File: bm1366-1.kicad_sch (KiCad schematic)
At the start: 64 parts, among them U1 25MHz, U13 ADP171AUJ-R7, U14 BM1366_mode1, U23 ADP171AUJ-R7

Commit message: added some DK part numbers
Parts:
- R6: DK (none) -> 311-10KJRCT-ND; PARTNO (none) -> RC0402JR-0710KL
- U13, U23: DK (none) -> 505-ADP171AUJZ-R7CT-ND; PARTNO (none) -> ADP171AUJZ-R7
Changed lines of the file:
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@@
+      (effects (font (size 1.27 1.27)) hide)
+    )
+    (property "DK" "505-ADP171AUJZ-R7CT-ND" (at 62.865 177.165 0)
+      (effects (font (size 1.27 1.27)) hide)
+    )
+    (property "PARTNO" "ADP171AUJZ-R7" (at 62.865 177.165 0)
       (effects (font (size 1.27 1.27)) hide)
     )
@@
       (effects (font (size 1.27 1.27)) hide)
     )
+    (property "DK" "505-ADP171AUJZ-R7CT-ND" (at 62.865 144.145 0)
+      (effects (font (size 1.27 1.27)) hide)
+    )
+    (property "PARTNO" "ADP171AUJZ-R7" (at 62.865 144.145 0)
+      (effects (font (size 1.27 1.27)) hide)
+    )
     (pin "1")
     (pin "2")
@@
       (effects (font (size 1.27 1.27)) hide)
     )
-    (property "DK" "" (at 18.415 92.71 0)
-      (effects (font (size 1.27 1.27)) hide)
-    )
-    (property "PARTNO" "" (at 18.415 92.71 0)
-      (effects (font (size 1.27 1.27)) hide)
-    )
+    (property "DK" "311-10KJRCT-ND" (at 18.415 92.71 0)
+      (effects (font (size 1.27 1.27)) hide)
+    )
+    (property "PARTNO" "RC0402JR-0710KL" (at 18.415 92.71 0)
+      (effects (font (size 1.27 1.27)) hide)
+    )

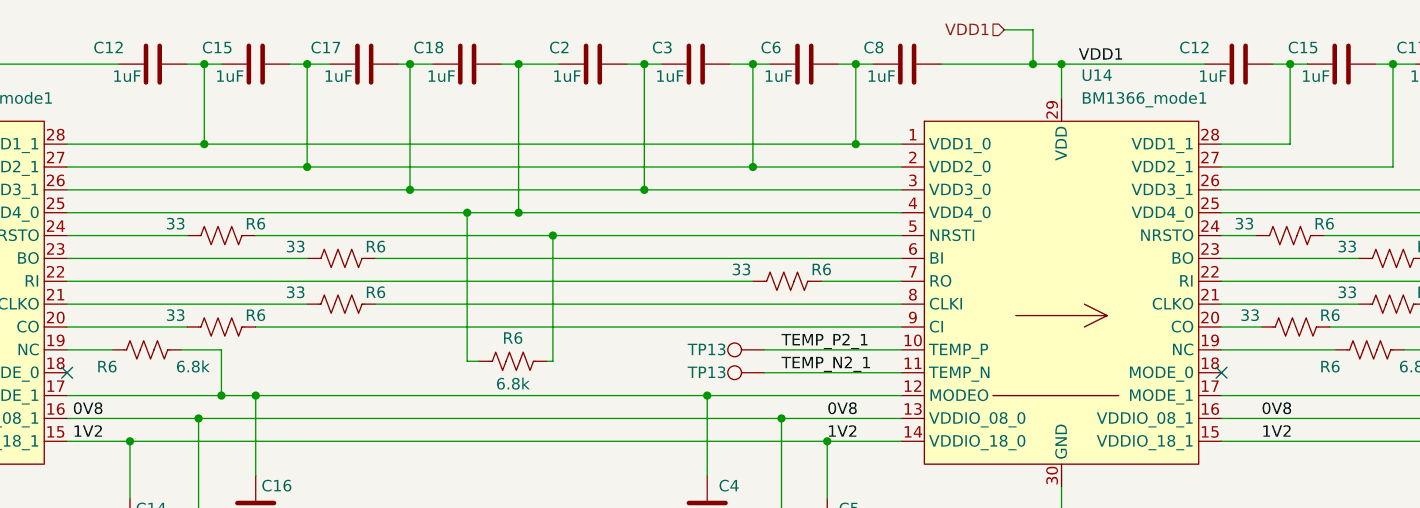
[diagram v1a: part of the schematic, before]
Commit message: Add ESP32 testpoints, fix all DRC errors
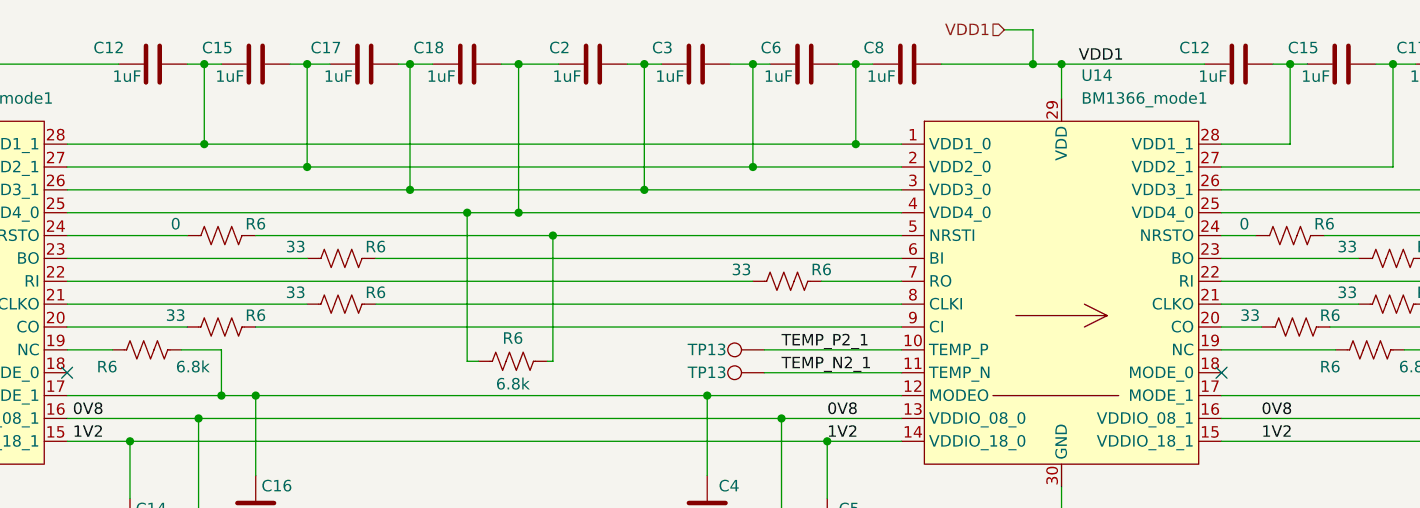
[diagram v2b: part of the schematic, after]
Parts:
- R6: value 33 -> 0
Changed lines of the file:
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@@
       (effects (font (size 1.27 1.27)))
     )
-    (property "Value" "33" (at 102.235 83.82 90)
+    (property "Value" "0" (at 102.235 83.82 90)
       (effects (font (size 1.27 1.27)))
     )
@@
       (effects (font (size 1.27 1.27)))
     )
-    (property "Value" "33" (at 220.98 83.82 90)
-      (effects (font (size 1.27 1.27)))
-    )
+    (property "Value" "0" (at 220.98 83.82 90)
+      (effects (font (size 1.27 1.27)))
+    )

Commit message: BOM mostly completed
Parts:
- R35, R36: DK (none) -> 311-1.00LRCT-ND; PARTNO (none) -> RC0402FR-071RL
- R6: value 130K -> 130k 1%; DK (none) -> YAG2969CT-ND; PARTNO (none) -> RC0402FR-07130KL; Tolerance 1% -> (none)
- R6: DK (none) -> 311-33.0LRCT-ND; PARTNO (none) -> RC0402FR-0733RL
- R6: DK (none) -> 13-RC0402FR-136K8LCT-ND; PARTNO (none) -> RC0402FR-136K8L
- R6: value 182K -> 182k 1%; DK (none) -> YAG3015CT-ND; PARTNO (none) -> RC0402FR-07182KL; Tolerance 1% -> (none)
- R6: DK (none) -> 311-0.0JRCT-ND; PARTNO (none) -> RC0402JR-070RL
- R6: value 309K -> 309k 1%; DK (none) -> YAG3108CT-ND; PARTNO (none) -> RC0402FR-07309KL; Tolerance 1% -> (none)
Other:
- title: bitaxeUltraHex -> bitaxeHex
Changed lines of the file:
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@@
   (paper "A")
   (title_block
-    (title "bitaxeUltraHex")
+    (title "bitaxeHex")
     (date "2023-06-11")
-    (rev "1")
+    (rev "300")
   )
   (junction (at 50.165 194.31) (diameter 0) (color 0 0 0 0)
@@
       (effects (font (size 1.27 1.27)))
     )
-    (property "Value" "130K" (at 71.12 189.865 0)
+    (property "Value" "130k 1%" (at 71.12 189.865 0)
       (effects (font (size 1.27 1.27)))
     )
@@
       (effects (font (size 1.27 1.27)) hide)
     )
-    (property "DK" "" (at 74.93 187.96 0)
+    (property "DK" "YAG2969CT-ND" (at 74.93 187.96 0)
       (effects (font (size 1.27 1.27)) hide)
     )
-    (property "PARTNO" "" (at 74.93 187.96 0)
+    (property "PARTNO" "RC0402FR-07130KL" (at 74.93 187.96 0)
       (effects (font (size 1.27 1.27)) hide)
     )
-    (property "Tolerance" "1%" (at 71.755 191.77 0)
-      (effects (font (size 1.27 1.27)))
-    )
     (pin "1")
     (pin "2")
@@
       (effects (font (size 1.27 1.27)) hide)
     )
-    (property "DK" "" (at 120.65 87.63 0)
+    (property "DK" "311-33.0LRCT-ND" (at 120.65 87.63 0)
       (effects (font (size 1.27 1.27)) hide)
     )
-    (property "PARTNO" "" (at 120.65 87.63 0)
+    (property "PARTNO" "RC0402FR-0733RL" (at 120.65 87.63 0)
       (effects (font (size 1.27 1.27)) hide)
     )
@@
       (effects (font (size 1.27 1.27)) hide)
     )
-    (property "DK" "" (at 139.7 99.06 0)
+    (property "DK" "13-RC0402FR-136K8LCT-ND" (at 139.7 99.06 0)
       (effects (font (size 1.27 1.27)) hide)
     )
-    (property "PARTNO" "" (at 139.7 99.06 0)
+    (property "PARTNO" "RC0402FR-136K8L" (at 139.7 99.06 0)
       (effects (font (size 1.27 1.27)) hide)
     )
@@
       (effects (font (size 1.27 1.27)) hide)
     )
-    (property "DK" "" (at 234.95 97.79 0)
+    (property "DK" "13-RC0402FR-136K8LCT-ND" (at 234.95 97.79 0)
       (effects (font (size 1.27 1.27)) hide)
     )
-    (property "PARTNO" "" (at 234.95 97.79 0)
+    (property "PARTNO" "RC0402FR-136K8L" (at 234.95 97.79 0)
       (effects (font (size 1.27 1.27)) hide)
     )
@@
       (effects (font (size 1.27 1.27)) hide)
     )
-    (property "DK" "" (at 99.06 97.79 0)
+    (property "DK" "13-RC0402FR-136K8LCT-ND" (at 99.06 97.79 0)
       (effects (font (size 1.27 1.27)) hide)
     )
-    (property "PARTNO" "" (at 99.06 97.79 0)
+    (property "PARTNO" "RC0402FR-136K8L" (at 99.06 97.79 0)
       (effects (font (size 1.27 1.27)) hide)
     )
@@
       (effects (font (size 1.27 1.27)))
     )
-    (property "Value" "182K" (at 81.28 183.515 90)
+    (property "Value" "182k 1%" (at 81.28 183.515 90)
       (effects (font (size 1.27 1.27)))
     )
@@
       (effects (font (size 1.27 1.27)) hide)
     )
-    (property "DK" "" (at 81.28 180.975 0)
+    (property "DK" "YAG3015CT-ND" (at 81.28 180.975 0)
       (effects (font (size 1.27 1.27)) hide)
     )
-    (property "PARTNO" "" (at 81.28 180.975 0)
+    (property "PARTNO" "RC0402FR-07182KL" (at 81.28 180.975 0)
       (effects (font (size 1.27 1.27)) hide)
     )
-    (property "Tolerance" "1%" (at 81.28 185.42 90)
-      (effects (font (size 1.27 1.27)))
-    )
     (pin "1")
     (pin "2")
@@
       (effects (font (size 1.27 1.27)) hide)
     )
-    (property "DK" "" (at 107.315 85.09 0)
+    (property "DK" "311-0.0JRCT-ND" (at 107.315 85.09 0)
       (effects (font (size 1.27 1.27)) hide)
     )
-    (property "PARTNO" "" (at 107.315 85.09 0)
+    (property "PARTNO" "RC0402JR-070RL" (at 107.315 85.09 0)
       (effects (font (size 1.27 1.27)) hide)
     )
@@
       (effects (font (size 1.27 1.27)) hide)
     )
+    (property "DK" "311-1.00LRCT-ND" (at 131.445 180.34 0)
+      (effects (font (size 1.27 1.27)) hide)
+    )
+    (property "PARTNO" "RC0402FR-071RL" (at 131.445 180.34 0)
+      (effects (font (size 1.27 1.27)) hide)
+    )
     (pin "1")
     (pin "2")
@@
       (effects (font (size 1.27 1.27)) hide)
     )
-    (property "DK" "" (at 237.49 87.63 0)
+    (property "DK" "311-33.0LRCT-ND" (at 237.49 87.63 0)
       (effects (font (size 1.27 1.27)) hide)
     )
-    (property "PARTNO" "" (at 237.49 87.63 0)
+    (property "PARTNO" "RC0402FR-0733RL" (at 237.49 87.63 0)
       (effects (font (size 1.27 1.27)) hide)
     )
@@
       (effects (font (size 1.27 1.27)) hide)
     )
-    (property "DK" "" (at 107.315 95.25 0)
+    (property "DK" "311-33.0LRCT-ND" (at 107.315 95.25 0)
       (effects (font (size 1.27 1.27)) hide)
     )
-    (property "PARTNO" "" (at 107.315 95.25 0)
+    (property "PARTNO" "RC0402FR-0733RL" (at 107.315 95.25 0)
       (effects (font (size 1.27 1.27)) hide)
     )
@@
       (effects (font (size 1.27 1.27)) hide)
     )
-    (property "DK" "" (at 120.65 92.71 0)
+    (property "DK" "311-33.0LRCT-ND" (at 120.65 92.71 0)
       (effects (font (size 1.27 1.27)) hide)
     )
-    (property "PARTNO" "" (at 120.65 92.71 0)
+    (property "PARTNO" "RC0402FR-0733RL" (at 120.65 92.71 0)
       (effects (font (size 1.27 1.27)) hide)
     )
@@
       (effects (font (size 1.27 1.27)) hide)
     )
-    (property "DK" "" (at 226.695 95.25 0)
+    (property "DK" "311-33.0LRCT-ND" (at 226.695 95.25 0)
       (effects (font (size 1.27 1.27)) hide)
     )
-    (property "PARTNO" "" (at 226.695 95.25 0)
+    (property "PARTNO" "RC0402FR-0733RL" (at 226.695 95.25 0)
       (effects (font (size 1.27 1.27)) hide)
     )
@@
       (effects (font (size 1.27 1.27)) hide)
     )
-    (property "DK" "" (at 226.06 85.09 0)
+    (property "DK" "311-0.0JRCT-ND" (at 226.06 85.09 0)
       (effects (font (size 1.27 1.27)) hide)
     )
-    (property "PARTNO" "" (at 226.06 85.09 0)
+    (property "PARTNO" "RC0402JR-070RL" (at 226.06 85.09 0)
       (effects (font (size 1.27 1.27)) hide)
     )
@@
       (effects (font (size 1.27 1.27)) hide)
     )
+    (property "DK" "311-1.00LRCT-ND" (at 122.555 180.34 0)
+      (effects (font (size 1.27 1.27)) hide)
+    )
+    (property "PARTNO" "RC0402FR-071RL" (at 122.555 180.34 0)
+      (effects (font (size 1.27 1.27)) hide)
+    )
     (pin "1")
     (pin "2")
@@
       (effects (font (size 1.27 1.27)) hide)
     )
-    (property "DK" "" (at 237.49 92.71 0)
+    (property "DK" "311-33.0LRCT-ND" (at 237.49 92.71 0)
       (effects (font (size 1.27 1.27)) hide)
     )
-    (property "PARTNO" "" (at 237.49 92.71 0)
+    (property "PARTNO" "RC0402FR-0733RL" (at 237.49 92.71 0)
       (effects (font (size 1.27 1.27)) hide)
     )
@@
       (effects (font (size 1.27 1.27)))
     )
-    (property "Value" "182K" (at 81.28 150.495 90)
+    (property "Value" "182k 1%" (at 81.28 150.495 90)
       (effects (font (size 1.27 1.27)))
     )
@@
       (effects (font (size 1.27 1.27)) hide)
     )
-    (property "DK" "" (at 81.28 147.955 0)
+    (property "DK" "YAG3015CT-ND" (at 81.28 147.955 0)
       (effects (font (size 1.27 1.27)) hide)
     )
-    (property "PARTNO" "" (at 81.28 147.955 0)
+    (property "PARTNO" "RC0402FR-07182KL" (at 81.28 147.955 0)
       (effects (font (size 1.27 1.27)) hide)
     )
-    (property "Tolerance" "1%" (at 81.28 152.4 90)
-      (effects (font (size 1.27 1.27)))
-    )
     (pin "1")
     (pin "2")
@@
       (effects (font (size 1.27 1.27)) hide)
     )
-    (property "DK" "" (at 170.18 90.17 0)
+    (property "DK" "311-33.0LRCT-ND" (at 170.18 90.17 0)
       (effects (font (size 1.27 1.27)) hide)
     )
-    (property "PARTNO" "" (at 170.18 90.17 0)
+    (property "PARTNO" "RC0402FR-0733RL" (at 170.18 90.17 0)
       (effects (font (size 1.27 1.27)) hide)
     )
@@
       (effects (font (size 1.27 1.27)))
     )
-    (property "Value" "309K" (at 71.12 156.845 0)
+    (property "Value" "309k 1%" (at 71.12 156.845 0)
       (effects (font (size 1.27 1.27)))
     )
@@
       (effects (font (size 1.27 1.27)) hide)
     )
-    (property "DK" "" (at 74.93 154.94 0)
+    (property "DK" "YAG3108CT-ND" (at 74.93 154.94 0)
       (effects (font (size 1.27 1.27)) hide)
     )
-    (property "PARTNO" "" (at 74.93 154.94 0)
+    (property "PARTNO" "RC0402FR-07309KL" (at 74.93 154.94 0)
       (effects (font (size 1.27 1.27)) hide)
     )
-    (property "Tolerance" "1%" (at 71.755 159.385 0)
-      (effects (font (size 1.27 1.27)))
-    )
     (pin "1")

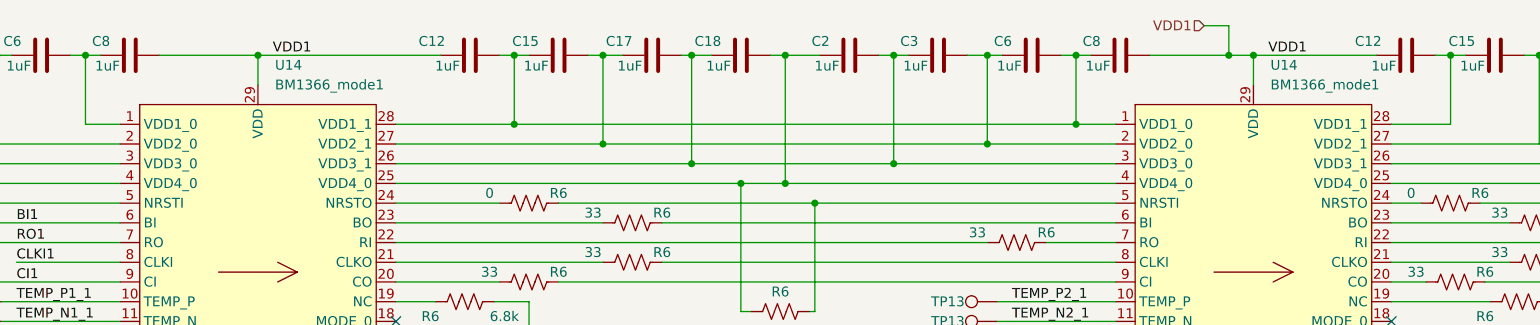
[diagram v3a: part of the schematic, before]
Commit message: link heatsink to schematic and re-link heatsink mounting holes :P
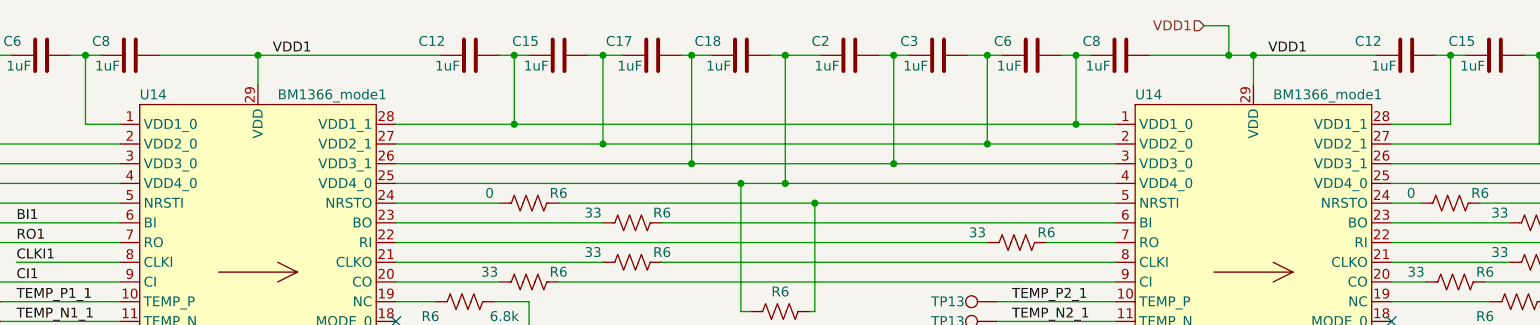
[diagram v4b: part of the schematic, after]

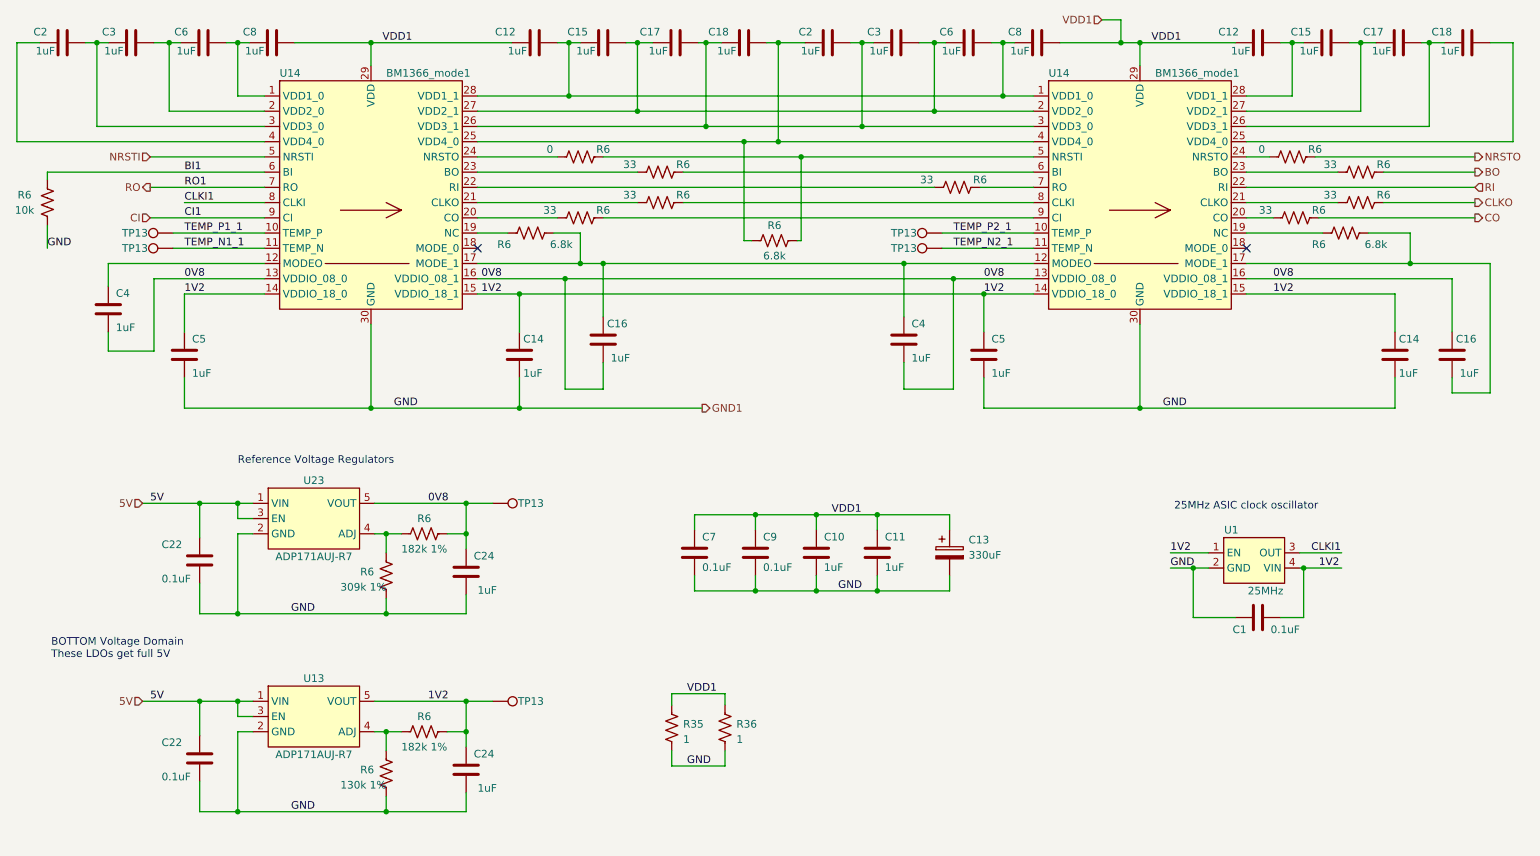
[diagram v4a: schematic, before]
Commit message: sorting out new info on the BM1366 pinouts
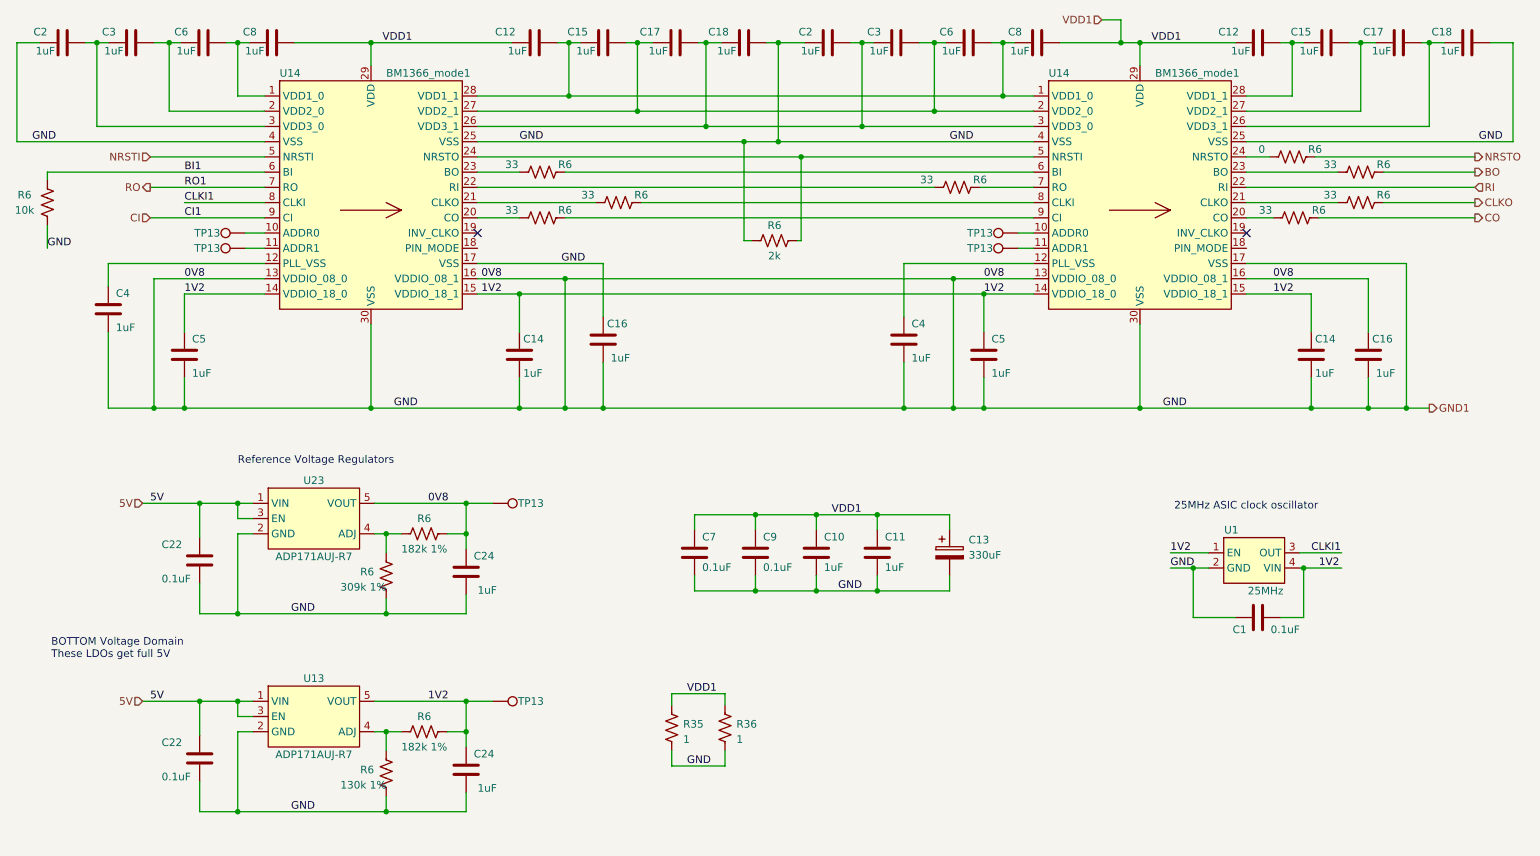
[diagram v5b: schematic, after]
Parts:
- removed R6 (x2): 6.8k, Resistor_SMD:R_0402_1005Metric, symbol Device:R_US
- removed R6: 0, Resistor_SMD:R_0402_1005Metric, symbol Device:R_US
- R6: value 6.8k -> 2k; DK 13-RC0402FR-136K8LCT-ND -> (none); PARTNO RC0402FR-136K8L -> (none)
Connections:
- net 0V8 is gone; now on net GND1: C16.1, C16.2, C24.1, C4.2, C4.2, R6.1, TP13.1, U14.13 (VDDIO_08_0), U14.13 (VDDIO_08_0), U14.16 (VDDIO_08_1), U14.16 (VDDIO_08_1), U23.5 (VOUT)
- net GND1: now also C16.1, C16.2, C18.2, C18.2, C2.1, C2.1, R6.1, U14.17 (VSS), U14.17 (VSS), U14.25 (VSS), U14.25 (VSS), U14.4 (VSS), U14.4 (VSS)
- net at C4.1, U14.12 (PLL_VSS): no longer C16.1, U14.17 (MODE_1)
- net at U14.24 (NRSTO): now also R6.2, U14.5 (NRSTI)
- net TEMP_N1_1: no longer names the net of TP13.1, U14.11 (ADDR1)
- net TEMP_N2_1: no longer names the net of TP13.1, U14.11 (ADDR1)
- net TEMP_P1_1: no longer names the net of TP13.1, U14.10 (ADDR0)
- net TEMP_P2_1: no longer names the net of TP13.1, U14.10 (ADDR0)
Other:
- moved on the sheet: C14, C16, R6, TP13
